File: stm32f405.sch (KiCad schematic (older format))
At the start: 17 parts, among them Q1 CRYSTAL_50X32, U1 STM32F405R

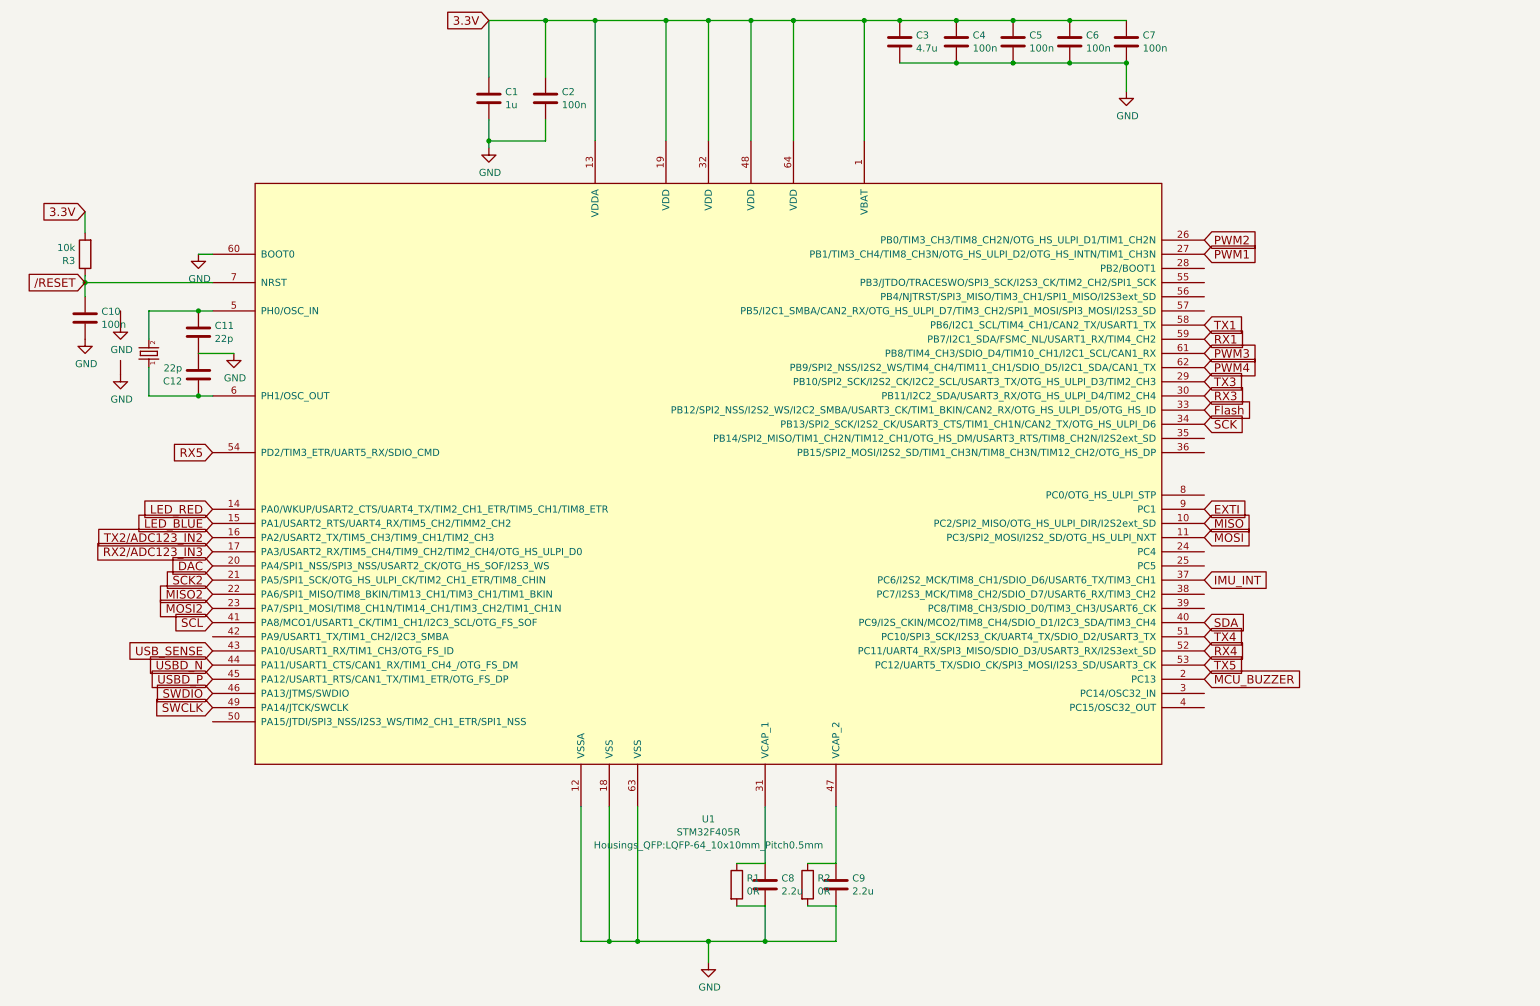
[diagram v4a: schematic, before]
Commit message: OSD running on breadboard
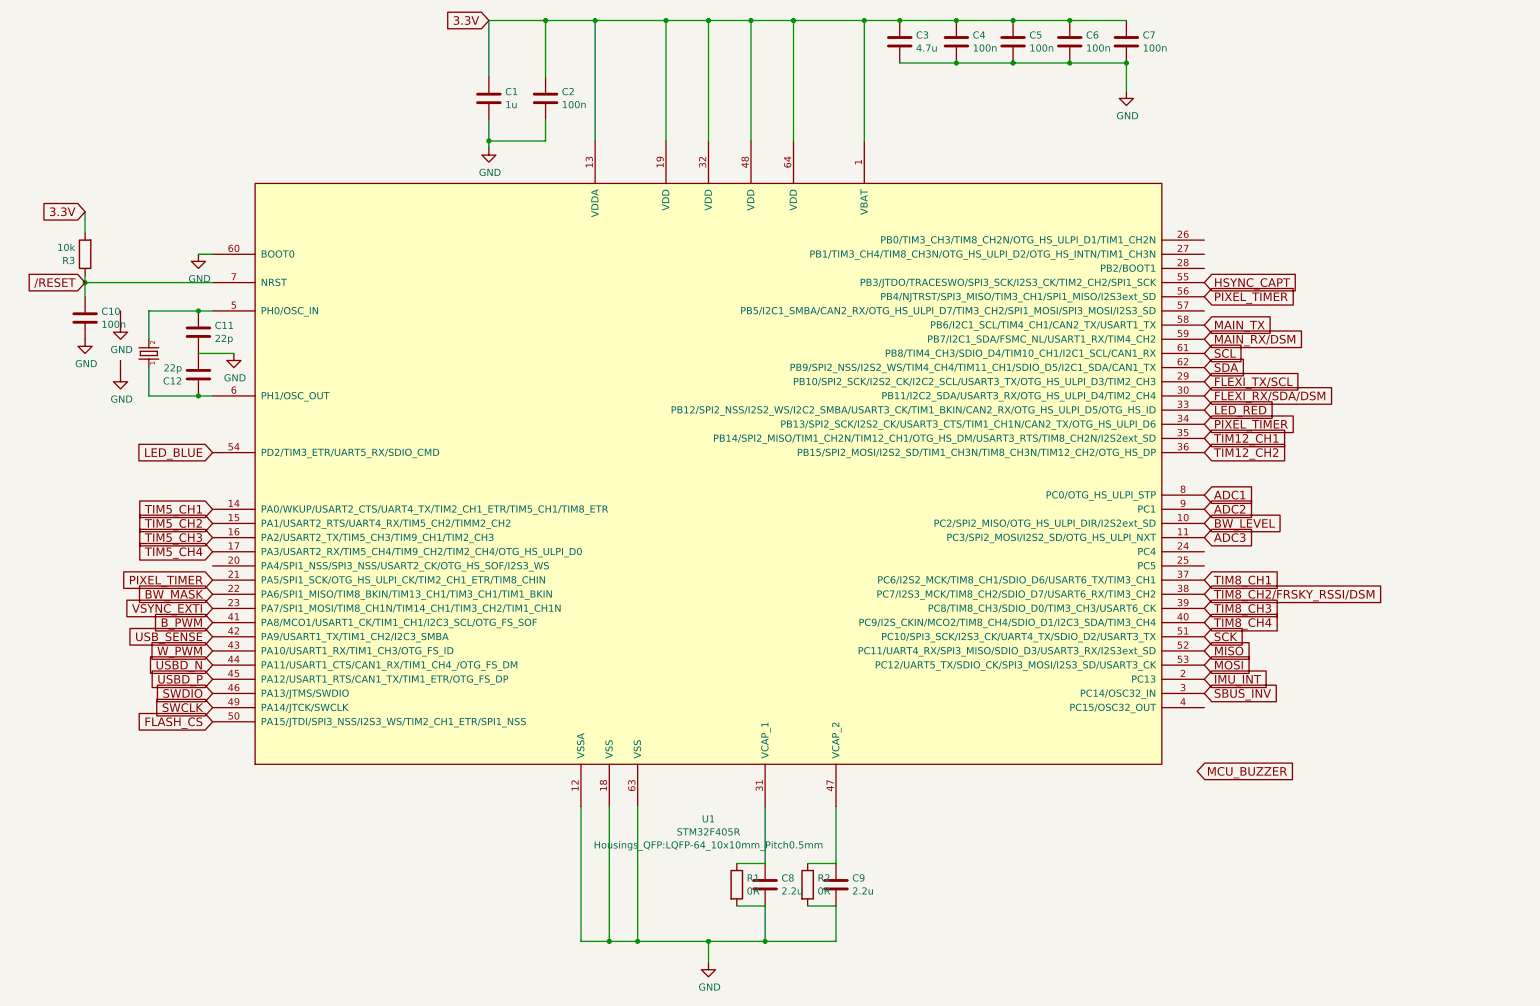
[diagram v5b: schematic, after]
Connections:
- net Flash is gone; now on net LED_RED: U1.33 (PB12/SPI2_NSS/I2S2_WS/I2C2_SMBA/USART3_CK/TIM1_BKIN/CAN2_RX/OTG_HS_ULPI_D5/OTG_HS_ID)
- net PWM3 is gone; now on net SCL: U1.61 (PB8/TIM4_CH3/SDIO_D4/TIM10_CH1/I2C1_SCL/CAN1_RX)
- net PWM4 is gone; now on net SDA: U1.62 (PB9/SPI2_NSS/I2S2_WS/TIM4_CH4/TIM11_CH1/SDIO_D5/I2C1_SDA/CAN1_TX)
- net RX4 is gone; now on net MISO: U1.52 (PC11/UART4_RX/SPI3_MISO/SDIO_D3/USART3_RX/I2S3ext_SD)
- net RX5 is gone; now on net LED_BLUE: U1.54 (PD2/TIM3_ETR/UART5_RX/SDIO_CMD)
- net SCK2 is gone; now on net PIXEL_TIMER: U1.21 (PA5/SPI1_SCK/OTG_HS_ULPI_CK/TIM2_CH1_ETR/TIM8_CHIN)
- net TX4 is gone; now on net SCK: U1.51 (PC10/SPI3_SCK/I2S3_CK/UART4_TX/SDIO_D2/USART3_TX)
- net TX5 is gone; now on net MOSI: U1.53 (PC12/UART5_TX/SDIO_CK/SPI3_MOSI/I2S3_SD/USART3_CK)
- net IMU_INT: now also U1.2 (PC13); no longer U1.37 (PC6/I2S2_MCK/TIM8_CH1/SDIO_D6/USART6_TX/TIM3_CH1)
- net LED_BLUE: no longer U1.15 (PA1/USART2_RTS/UART4_RX/TIM5_CH2/TIMM2_CH2)
- net LED_RED: no longer U1.14 (PA0/WKUP/USART2_CTS/UART4_TX/TIM2_CH1_ETR/TIM5_CH1/TIM8_ETR)
- net MCU_BUZZER: no longer U1.2 (PC13)
- net MISO: no longer U1.10 (PC2/SPI2_MISO/OTG_HS_ULPI_DIR/I2S2ext_SD)
- net MOSI: no longer U1.11 (PC3/SPI2_MOSI/I2S2_SD/OTG_HS_ULPI_NXT)
- net SCK: no longer U1.34 (PB13/SPI2_SCK/I2S2_CK/USART3_CTS/TIM1_CH1N/CAN2_TX/OTG_HS_ULPI_D6)
- net SCL: no longer U1.41 (PA8/MCO1/USART1_CK/TIM1_CH1/I2C3_SCL/OTG_FS_SOF)
- net SDA: no longer U1.40 (PC9/I2S_CKIN/MCO2/TIM8_CH4/SDIO_D1/I2C3_SDA/TIM3_CH4)
- net USB_SENSE: now also U1.42 (PA9/USART1_TX/TIM1_CH2/I2C3_SMBA); no longer U1.43 (PA10/USART1_RX/TIM1_CH3/OTG_FS_ID)
- net SBUS_INV: now reaches U1.3 (PC14/OSC32_IN)
- net TIM12_CH1: now reaches U1.35 (PB14/SPI2_MISO/TIM1_CH2N/TIM12_CH1/OTG_HS_DM/USART3_RTS/TIM8_CH2N/I2S2ext_SD)
- net TIM12_CH2: now reaches U1.36 (PB15/SPI2_MOSI/I2S2_SD/TIM1_CH3N/TIM8_CH3N/TIM12_CH2/OTG_HS_DP)
- net TIM8_CH2/FRSKY_RSSI/DSM: now reaches U1.38 (PC7/I2S3_MCK/TIM8_CH2/SDIO_D7/USART6_RX/TIM3_CH2)
- net TIM8_CH3: now reaches U1.39 (PC8/TIM8_CH3/SDIO_D0/TIM3_CH3/USART6_CK)
- net FLASH_CS: now reaches U1.50 (PA15/JTDI/SPI3_NSS/I2S3_WS/TIM2_CH1_ETR/SPI1_NSS)
- net HSYNC_CAPT: now reaches U1.55 (PB3/JTDO/TRACESWO/SPI3_SCK/I2S3_CK/TIM2_CH2/SPI1_SCK)
- net PIXEL_TIMER: now reaches U1.56 (PB4/NJTRST/SPI3_MISO/TIM3_CH1/SPI1_MISO/I2S3ext_SD)
- net PIXEL_TIMER: now also U1.34 (PB13/SPI2_SCK/I2S2_CK/USART3_CTS/TIM1_CH1N/CAN2_TX/OTG_HS_ULPI_D6)
- net ADC1: now reaches U1.8 (PC0/OTG_HS_ULPI_STP)
- net DAC: no longer names the net of U1.20 (PA4/SPI1_NSS/SPI3_NSS/USART2_CK/OTG_HS_SOF/I2S3_WS)
- net EXTI renamed ADC2
- net MISO2 renamed BW_MASK
- net MOSI2 renamed VSYNC_EXTI
- net PWM1: no longer names the net of U1.27 (PB1/TIM3_CH4/TIM8_CH3N/OTG_HS_ULPI_D2/OTG_HS_INTN/TIM1_CH3N)
- net PWM2: no longer names the net of U1.26 (PB0/TIM3_CH3/TIM8_CH2N/OTG_HS_ULPI_D1/TIM1_CH2N)
- net RX1 renamed MAIN_RX/DSM
- net RX2/ADC123_IN3 renamed TIM5_CH4
- net RX3 renamed FLEXI_RX/SDA/DSM
- net TX1 renamed MAIN_TX
- net TX2/ADC123_IN2 renamed TIM5_CH3
- net TX3 renamed FLEXI_TX/SCL
- new net ADC3: U1.11 (PC3/SPI2_MOSI/I2S2_SD/OTG_HS_ULPI_NXT)
- new net BW_LEVEL: U1.10 (PC2/SPI2_MISO/OTG_HS_ULPI_DIR/I2S2ext_SD)
- new net B_PWM: U1.41 (PA8/MCO1/USART1_CK/TIM1_CH1/I2C3_SCL/OTG_FS_SOF)
- new net TIM5_CH1: U1.14 (PA0/WKUP/USART2_CTS/UART4_TX/TIM2_CH1_ETR/TIM5_CH1/TIM8_ETR)
- new net TIM5_CH2: U1.15 (PA1/USART2_RTS/UART4_RX/TIM5_CH2/TIMM2_CH2)
- new net TIM8_CH1: U1.37 (PC6/I2S2_MCK/TIM8_CH1/SDIO_D6/USART6_TX/TIM3_CH1)
- new net TIM8_CH4: U1.40 (PC9/I2S_CKIN/MCO2/TIM8_CH4/SDIO_D1/I2C3_SDA/TIM3_CH4)
- new net W_PWM: U1.43 (PA10/USART1_RX/TIM1_CH3/OTG_FS_ID)
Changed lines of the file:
@@
 Comment4 ""
 $EndDescr
-Text GLabel 9050 3600 2    60   Input ~ 0
+Text GLabel 9050 5100 2    60   Input ~ 0
 SCK
-Text GLabel 9050 3500 2    60   Input ~ 0
-Flash
-Text GLabel 9050 3400 2    60   Input ~ 0
-RX3
-Text GLabel 9050 3300 2    60   Input ~ 0
-TX3
-Text GLabel 9050 3200 2    60   Input ~ 0
-PWM4
-Text GLabel 9050 3100 2    60   Input ~ 0
-PWM3
-Text GLabel 9050 3000 2    60   Input ~ 0
-RX1
+Text GLabel 2050 5700 0    60   Input ~ 0
+FLASH_CS
+Text GLabel 9050 4100 2    60   Input ~ 0
+ADC1
+Text GLabel 9050 3700 2    60   Input ~ 0
+TIM12_CH1
+Text GLabel 2050 4500 0    60   Input ~ 0
+TIM5_CH4
+Text GLabel 2050 4400 0    60   Input ~ 0
+TIM5_CH3
 Text GLabel 9050 2900 2    60   Input ~ 0
-TX1
-Text GLabel 9050 2400 2    60   Input ~ 0
-PWM1
-Text GLabel 9050 2300 2    60   Input ~ 0
-PWM2
+MAIN_TX
+Text GLabel 2050 4200 0    60   Input ~ 0
+TIM5_CH1
+Text GLabel 2050 4300 0    60   Input ~ 0
+TIM5_CH2
 $Comp
 L C C4
@@
 $EndComp
 $Comp
-L GND #PWR016
+L GND #PWR020
 U 1 1 569AE259
 P 5550 7400
-F 0 "#PWR016" H 5550 7150 50  0001 C CNN
+F 0 "#PWR020" H 5550 7150 50  0001 C CNN
 F 1 "GND" H 5558 7226 50  0000 C CNN
 F 2 "" H 5550 7400 50  0000 C CNN
@@
 $EndComp
 $Comp
-L GND #PWR017
+L GND #PWR021
 U 1 1 569AE27B
 P 4000 1650
-F 0 "#PWR017" H 4000 1400 50  0001 C CNN
+F 0 "#PWR021" H 4000 1400 50  0001 C CNN
 F 1 "GND" H 4008 1476 50  0000 C CNN
 F 2 "" H 4000 1650 50  0000 C CNN
@@
 $EndComp
 $Comp
-L GND #PWR018
+L GND #PWR022
 U 1 1 569AE29F
 P 1150 3000
-F 0 "#PWR018" H 1150 2750 50  0001 C CNN
+F 0 "#PWR022" H 1150 2750 50  0001 C CNN
 F 1 "GND" H 1158 2826 50  0000 C CNN
 F 2 "" H 1150 3000 50  0000 C CNN
@@
 $EndComp
 $Comp
-L GND #PWR019
+L GND #PWR023
 U 1 1 569AE2B7
 P 1400 2900
-F 0 "#PWR019" H 1400 2650 50  0001 C CNN
+F 0 "#PWR023" H 1400 2650 50  0001 C CNN
 F 1 "GND" H 1408 2726 50  0000 C CNN
 F 2 "" H 1400 2900 50  0000 C CNN
@@
 $EndComp
 $Comp
-L GND #PWR020
+L GND #PWR024
 U 1 1 569AE2BD
 P 1400 3250
-F 0 "#PWR020" H 1400 3000 50  0001 C CNN
+F 0 "#PWR024" H 1400 3000 50  0001 C CNN
 F 1 "GND" H 1408 3076 50  0000 C CNN
 F 2 "" H 1400 3250 50  0000 C CNN
@@
 $EndComp
 $Comp
-L GND #PWR021
+L GND #PWR025
 U 1 1 569AE2D1
 P 2200 3100
-F 0 "#PWR021" H 2200 2850 50  0001 C CNN
+F 0 "#PWR025" H 2200 2850 50  0001 C CNN
 F 1 "GND" H 2208 2926 50  0000 C CNN
 F 2 "" H 2200 3100 50  0000 C CNN
@@
 	1    0    0    -1
 $EndComp
-Text GLabel 2050 3800 0    60   Input ~ 0
-RX5
-Text GLabel 2050 4400 0    60   Input ~ 0
-TX2/ADC123_IN2
-Text GLabel 2050 4500 0    60   Input ~ 0
-RX2/ADC123_IN3
-Text GLabel 2050 4600 0    60   Input ~ 0
-DAC
-Text GLabel 2050 4700 0    60   Input ~ 0
-SCK2
-Text GLabel 2050 4800 0    60   Input ~ 0
-MISO2
-Text GLabel 2050 4900 0    60   Input ~ 0
-MOSI2
-Text GLabel 2050 5000 0    60   Input ~ 0
+Text GLabel 9050 4800 2    60   Input ~ 0
+TIM8_CH2/FRSKY_RSSI/DSM
+Text GLabel 9050 4200 2    60   Input ~ 0
+ADC2
+Text GLabel 9050 4400 2    60   Input ~ 0
+ADC3
+Text GLabel 9050 5500 2    60   Input ~ 0
+SBUS_INV
+Text GLabel 9050 3300 2    60   Input ~ 0
+FLEXI_TX/SCL
+Text GLabel 9050 3000 2    60   Input ~ 0
+MAIN_RX/DSM
+Text GLabel 9050 3400 2    60   Input ~ 0
+FLEXI_RX/SDA/DSM
+Text GLabel 9050 3100 2    60   Input ~ 0
 SCL
 Text GLabel 2050 5300 0    60   Input ~ 0
@@
 Text GLabel 1150 2600 0    60   Input ~ 0
 /RESET
-Text GLabel 9050 5400 2    60   Input ~ 0
+Text GLabel 9000 6050 2    60   Input ~ 0
 MCU_BUZZER
-Text GLabel 9050 4200 2    60   Input ~ 0
-EXTI
-Text GLabel 9050 4300 2    60   Input ~ 0
+Text GLabel 9050 3800 2    60   Input ~ 0
+TIM12_CH2
+Text GLabel 9050 5200 2    60   Input ~ 0
 MISO
-Text GLabel 9050 4400 2    60   Input ~ 0
+Text GLabel 9050 5300 2    60   Input ~ 0
 MOSI
+Text GLabel 9050 3200 2    60   Input ~ 0
+SDA
+Text GLabel 9050 4700 2    60   Input ~ 0
+TIM8_CH1
 Text GLabel 9050 5000 2    60   Input ~ 0
-SDA
-Text GLabel 9050 5100 2    60   Input ~ 0
-TX4
-Text GLabel 9050 5200 2    60   Input ~ 0
-RX4
-Text GLabel 9050 5300 2    60   Input ~ 0
-TX5
-Text GLabel 2050 4200 0    60   Input ~ 0
+TIM8_CH4
+Text GLabel 9050 4900 2    60   Input ~ 0
+TIM8_CH3
+Text GLabel 9050 3500 2    60   Input ~ 0
 LED_RED
-Text GLabel 2050 4300 0    60   Input ~ 0
+Text GLabel 2050 3800 0    60   Input ~ 0
 LED_BLUE
 $Comp
@@
 	4000 750  8500 750
 $Comp
-L GND #PWR022
+L GND #PWR026
 U 1 1 569E1F9F
 P 1950 2400
-F 0 "#PWR022" H 1950 2150 50  0001 C CNN
+F 0 "#PWR026" H 1950 2150 50  0001 C CNN
 F 1 "GND" H 1958 2226 50  0000 C CNN
 F 2 "" H 1950 2400 50  0000 C CNN
@@
 Connection ~ 6900 750
 $Comp
-L GND #PWR023
+L GND #PWR027
 U 1 1 569E5F3D
 P 8500 1250
-F 0 "#PWR023" H 8500 1000 50  0001 C CNN
+F 0 "#PWR027" H 8500 1000 50  0001 C CNN
 F 1 "GND" H 8508 1076 50  0000 C CNN
 F 2 "" H 8500 1250 50  0000 C CNN
@@
 	6650 1600 6650 750
 Connection ~ 6650 750
-Text GLabel 9050 4700 2    60   Input ~ 0
+Text GLabel 9050 5400 2    60   Input ~ 0
 IMU_INT
+Text GLabel 2050 5100 0    60   Input ~ 0
+USB_SENSE
+Text GLabel 9050 2600 2    60   Input ~ 0
+HSYNC_CAPT
+Text GLabel 9050 2700 2    60   Input ~ 0
+PIXEL_TIMER
+Text GLabel 9050 3600 2    60   Input ~ 0
+PIXEL_TIMER
+Text GLabel 2050 4700 0    60   Input ~ 0
+PIXEL_TIMER
+Text GLabel 9050 4300 2    60   Input ~ 0
+BW_LEVEL
+Text GLabel 2050 4800 0    60   Input ~ 0
+BW_MASK
+Text GLabel 2050 4900 0    60   Input ~ 0
+VSYNC_EXTI
+Text GLabel 2050 5000 0    60   Input ~ 0
+B_PWM
 Text GLabel 2050 5200 0    60   Input ~ 0
-USB_SENSE
+W_PWM
 $EndSCHEMATC
